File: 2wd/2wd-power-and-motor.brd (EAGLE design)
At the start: 100 x 80 mm, 10 parts, among them J2 To Motherboard, J3 Right Motor, J4 Left Motor

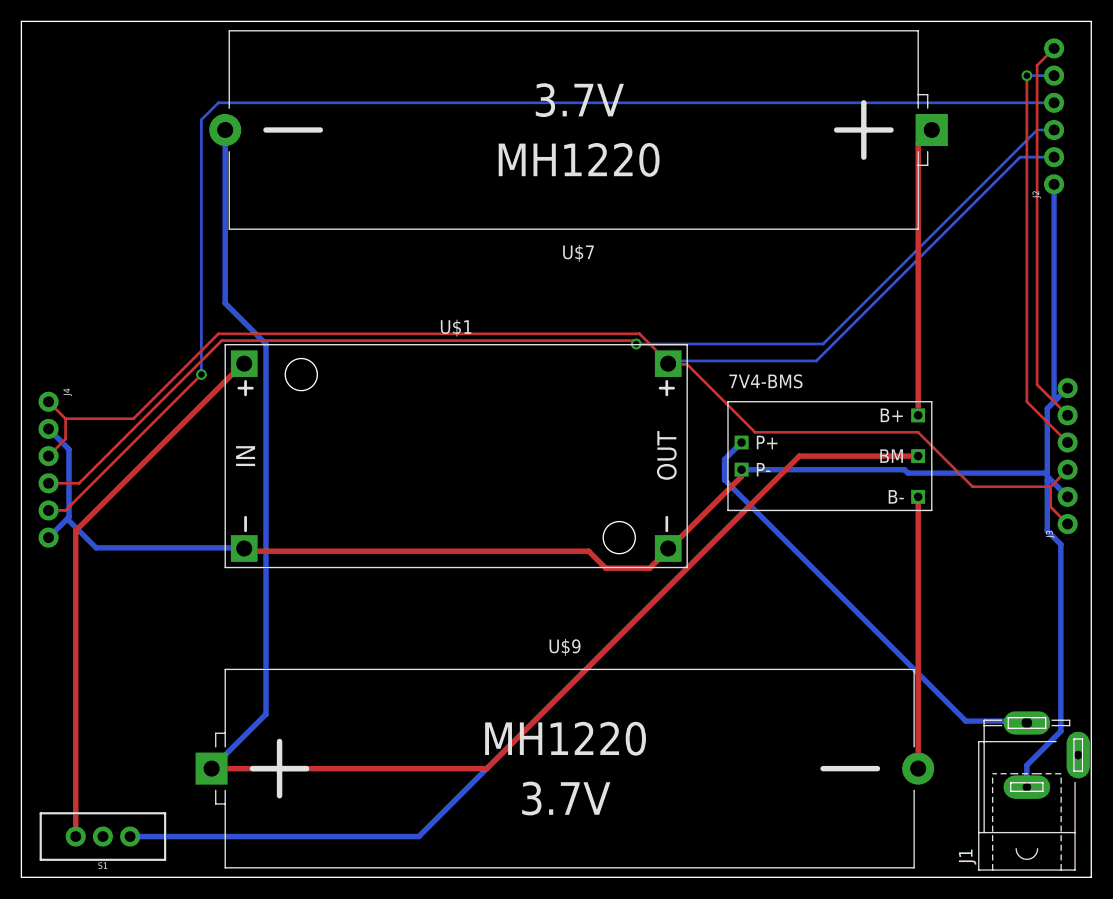
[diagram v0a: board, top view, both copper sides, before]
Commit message: Resized board, added motor driver.
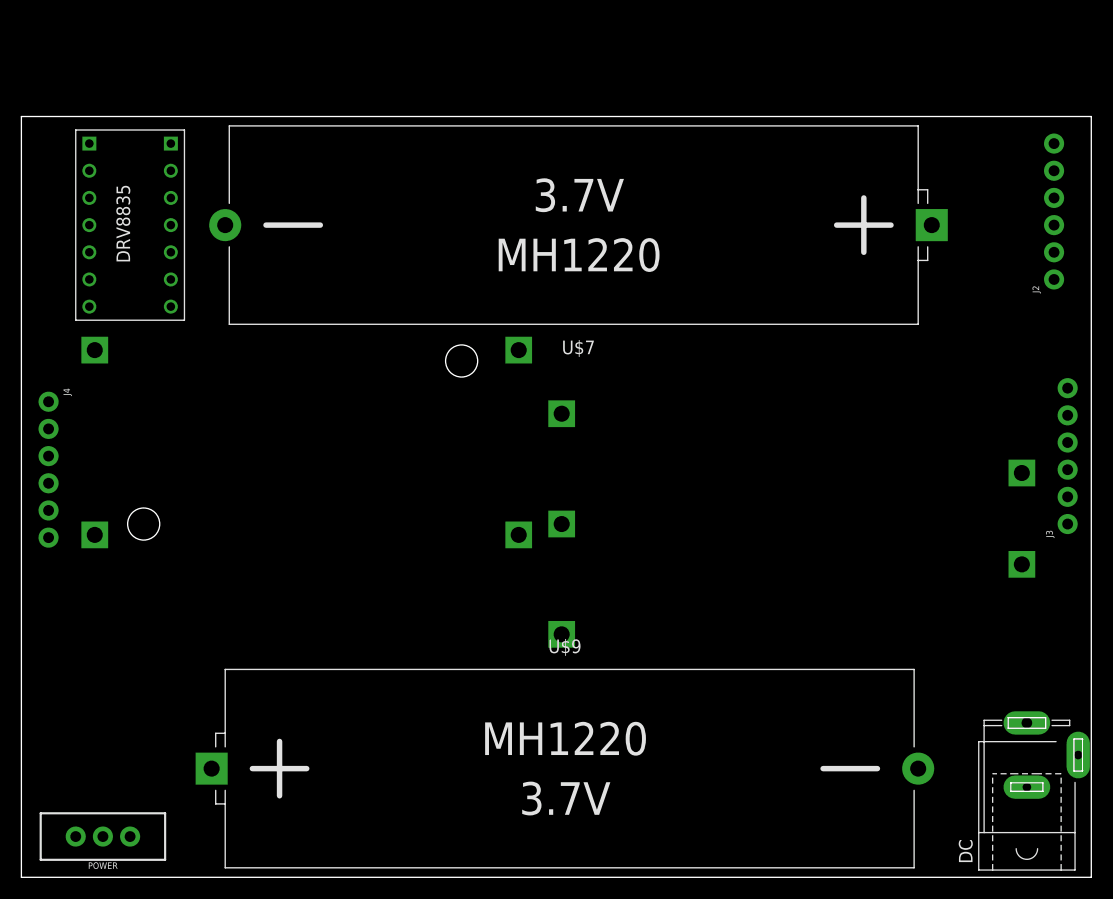
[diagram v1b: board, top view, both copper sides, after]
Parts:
- added U$2: POLOLU_MOTOR_DRV8835THROUGHHOLE, pololu:POLOLU_MOTOR_DRV_DRV8835
- DC: value (none) -> 9V
- moved U$1 14.0 mm to (26.7, 40.6), flipped to the bottom
- moved J2 8.89 mm to (96.5, 55.9)
- moved U$7 8.89 mm to (52.1, 61.0)
- moved 7V4-BMS 6.84 mm to (72.4, 33.0), flipped to the bottom
- renumbered J1 to DC, S1 to POWER
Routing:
- net GND: track 172.4 -> 0.00 mm
- net N$2: track 158.2 -> 0.00 mm
- net N$6: track 141.5 -> 0.00 mm
- net LB: track 123.7 -> 0.00 mm, vias 1 -> 0
- net N$3: track 112.7 -> 0.00 mm
- net LA: track 107.9 -> 0.00 mm, vias 1 -> 0
- net N$1: track 50.8 -> 0.00 mm
- net RA: track 38.4 -> 0.00 mm, vias 1 -> 0
- net RB: track 36.1 -> 0.00 mm
- net N$4: track 27.2 -> 0.00 mm
- net N$5: track 25.4 -> 0.00 mm
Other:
- board size 100 x 80 mm -> 100 x 71.1 mm

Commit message: Added integrated voltage regulation
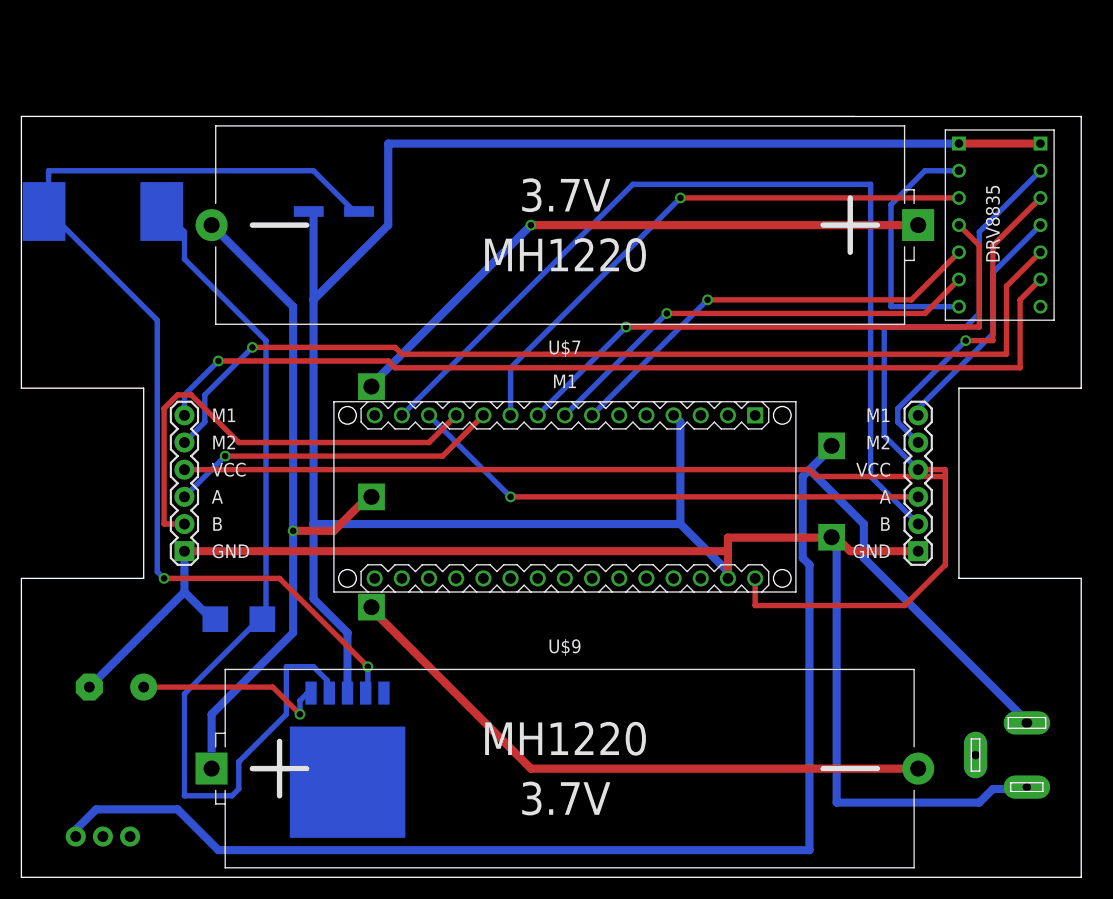
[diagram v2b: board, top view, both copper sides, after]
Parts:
- removed 7V4-BMS: BMS, tiogaplanet:BMS
- removed J2: To Motherboard, SparkFun-Connectors:1X06_NO_SILK
- removed J3: Right Motor, SparkFun-Connectors:1X06_NO_SILK
- removed J4: Left Motor, SparkFun-Connectors:1X06_NO_SILK
- removed U$1: DC-DC-STEP-DOWN-LM2596, diy-modules:DC-DC-STEP-DOWN-LM2596
- added C1: 680uF, rcl:E5-10,5
- added C2: 220uF, rcl:UD-6,3X5,8_NICHICON
- added D1: 1N5824, diode:SMB
- added IC1: LM2596S, national-semiconductor:TO263-5
- added J1: (no value), tiogaplanet:LEFT_MOTOR_CONN
- added J5: (no value), tiogaplanet:RIGHT_MOTOR_CONN
- added L1: CDRH127/LD, inductor-sumida:CDRH127/LD
- added M1: ARDUINO-NANO-3.0-SOCKET, tiogaplanet:ARDUINO-NANO-3.0-SOCKET
- added U$3: BATTERY-MANAGEMENT-SYSTEM, tiogaplanet:BATTERY-MANAGEMENT-SYSTEM
- moved U$2 81.3 mm to (86.4, 52.1)
- moved U$7 1.27 mm to (50.8, 61.0)
- flipped DC to the bottom
- flipped POWER to the bottom
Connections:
- removed net N$2: J2.2, J3.1, J3.3, J4.1, J4.3, U$1.OUT+
- new net +5V: J1.4, J5.4, M1.J2.1, U$2.VIN
- new net 3V3: M1.J2.14
- new net 5V: M1.J2.4
- new net AENBL: M1.J1.7, U$2.AENBL
- new net APHASE: M1.J1.8, U$2.APHASE
- new net BENBL: M1.J1.10, U$2.BENBL
- new net BPHASE: M1.J1.9, U$2.BPHASE
- new net FB: C2.+, IC1.4, L1.2
- new net LM1: J1.6, U$2.AOUT1
- new net LM2: J1.5, U$2.AOUT2
- new net N$10: U$2.MODE, U$2.VCC
- new net OUT: D1.C, IC1.2, L1.1
- new net RM1: J5.6, U$2.BOUT1
- new net RM2: J5.5, U$2.BOUT2
- new net VIN1: C1.+, IC1.1
- net GND: now also C1.-, C2.-, D1.A, IC1.3, J1.1, J5.1, M1.J1.4, M1.J2.2, U$2.LGND, U$2.MGND, U$3.P-; no longer 7V4-BMS.P-, J2.1, J3.2, J3.6, J4.2, J4.6, U$1.IN-, U$1.OUT-
- net LA: now also J1.3, M1.J1.11; no longer J2.3, J4.4
- net LB: now also J1.2, M1.J1.12; no longer J2.4, J4.5
- net N$1: no longer U$1.IN+
- net N$3: now also U$3.P+; no longer 7V4-BMS.P+
- net N$4: now also U$3.B+; no longer 7V4-BMS.B+
- net N$5: now also U$3.B-; no longer 7V4-BMS.B-
- net N$6: now also U$3.BM; no longer 7V4-BMS.BM
- net RA: now also J5.3, M1.J1.13; no longer J2.5, J3.4
- net RB: now also J5.2, M1.J1.14; no longer J2.6, J3.5
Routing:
- net GND: track 0.00 -> 313.8 mm
- net +5V: track 0.00 -> 144.5 mm
- net N$3: track 0.00 -> 142.8 mm
- net FB: track 0.00 -> 98.6 mm, vias 0 -> 2
- net LM2: track 0.00 -> 93.1 mm, vias 0 -> 1
- net LM1: track 0.00 -> 90.6 mm, vias 0 -> 1
- net OUT: track 0.00 -> 86.5 mm
- net RB: track 0.00 -> 86.3 mm
- net N$6: track 0.00 -> 65.7 mm, vias 0 -> 1
- net N$5: track 0.00 -> 57.4 mm
- net N$4: track 0.00 -> 57.4 mm, vias 0 -> 1
- net BPHASE: track 0.00 -> 55.0 mm, vias 0 -> 1
- net BENBL: track 0.00 -> 52.9 mm, vias 0 -> 1
- net RA: track 0.00 -> 48.9 mm, vias 0 -> 1
- net LB: track 0.00 -> 43.4 mm
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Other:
- board size 100 x 71.1 mm -> 99.1 x 71.1 mm
